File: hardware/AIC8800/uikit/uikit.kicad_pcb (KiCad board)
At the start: 2 copper layers, 50.8 x 69.2 mm, 50 parts, among them J1 Conn_01x20, J2 Conn_01x20, J3 Conn_01x10, J4 Conn_01x06, J5 USB_C_Receptacle_USB2.0, J6 Micro_SD_Card_Det, J7 PJ-393-USA, J8 Conn_01x02, SW0 SW_Push, U1 AIC1000A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

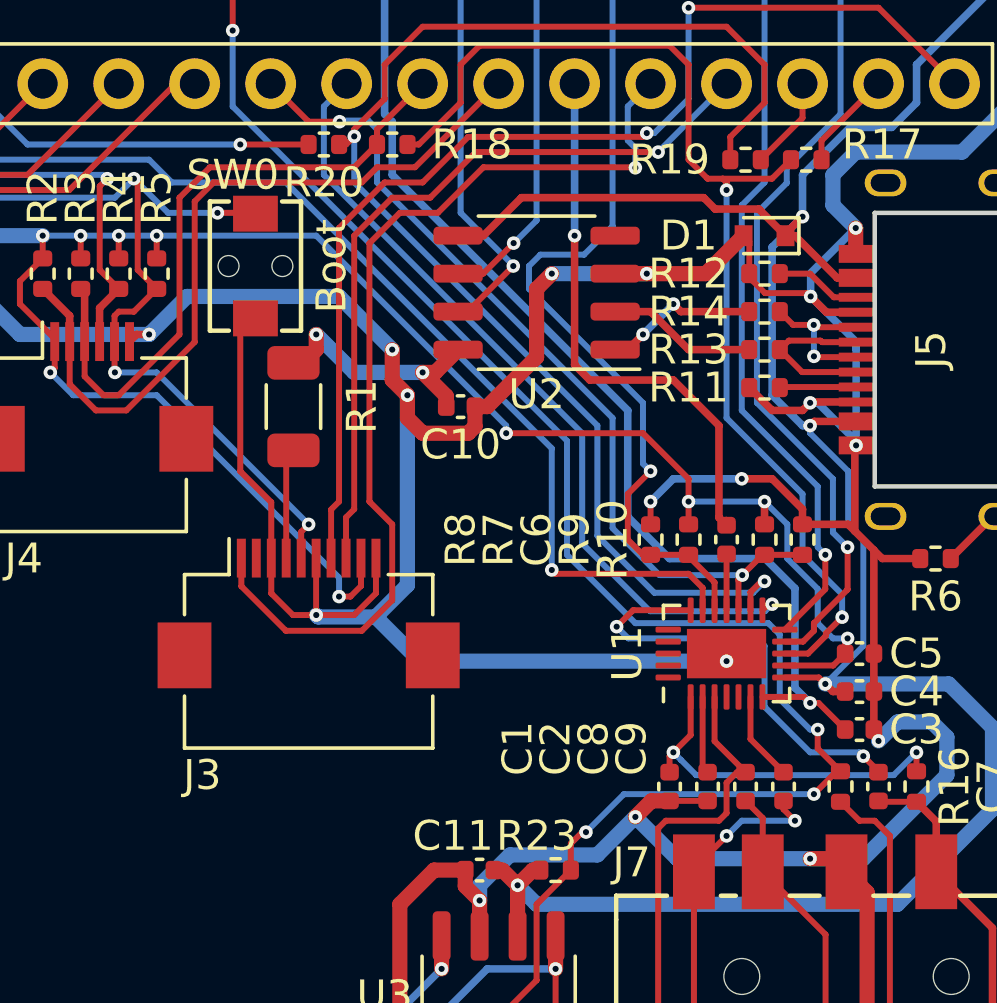
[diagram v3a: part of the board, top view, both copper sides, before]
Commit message: [hardware/aic8800m/uikit] add pin for debug uart
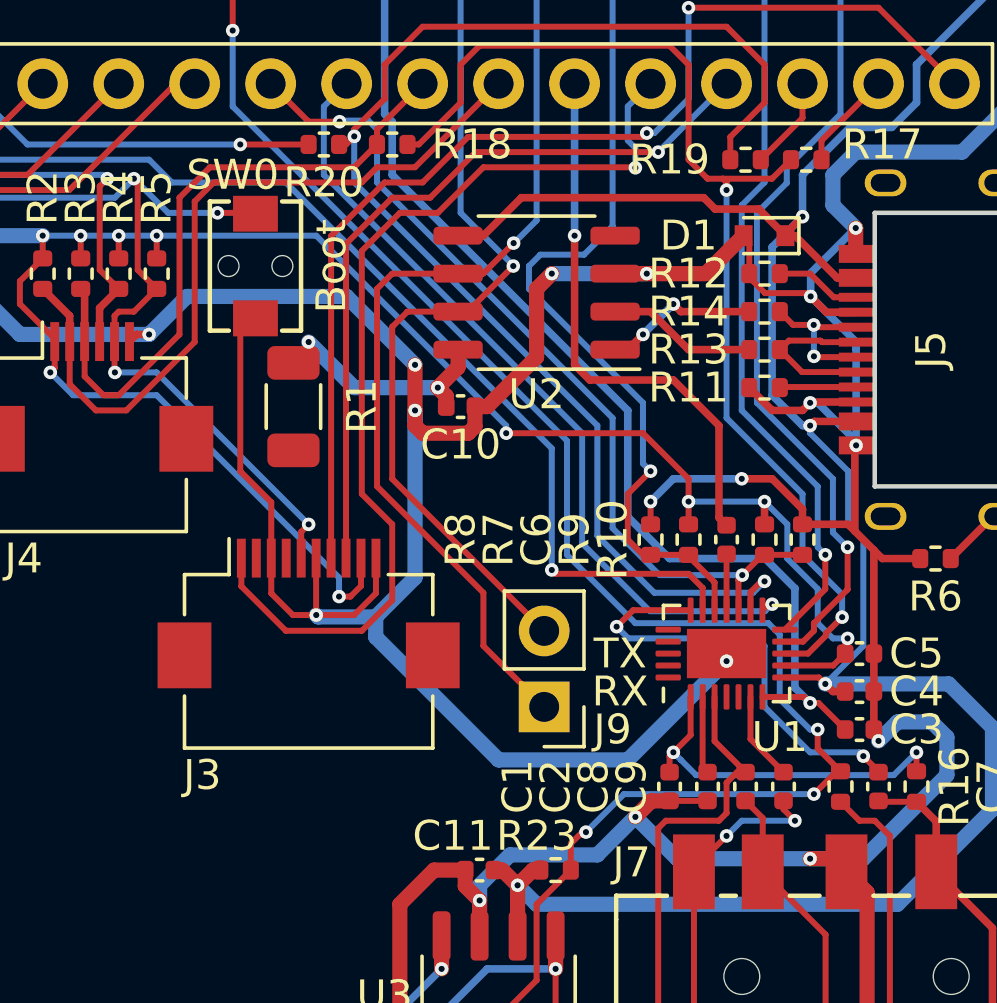
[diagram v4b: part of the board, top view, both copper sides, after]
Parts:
- added J9: Conn_01x02, Connector_PinHeader_2.54mm:PinHeader_1x02_P2.54mm_Vertical, F.Cu at (236.5, 136.4)
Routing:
- net /B2: track 33.9 -> 53.1 mm
- net /B3: track 35.3 -> 49.9 mm
- net /BL_A: track 3.70 -> 0.00 mm
- net GND: track 255.7 -> 258.6 mm
- net /USB_3V: track 8.51 -> 7.25 mm
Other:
- board text added: "RX"
- board text added: "TX"

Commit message: [hardware/aic8800m/uikit] update
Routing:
- net /BL_A: track 0.00 -> 3.70 mm
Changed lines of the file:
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@@
   (segment (start 212.09 115.57) (end 207.237 120.423) (width 0.2) (layer "F.Cu") (net 46))
   (segment (start 207.237 120.423) (end 204.354 120.423) (width 0.2) (layer "F.Cu") (net 46))
+  (segment (start 227.85 128.0695) (end 228.092 127.8275) (width 0.2) (layer "F.Cu") (net 49))
+  (segment (start 227.85 131.43) (end 227.85 128.0695) (width 0.2) (layer "F.Cu") (net 49))
   (segment (start 246.154 122.71) (end 246.9011 122.71) (width 0.2) (layer "F.Cu") (net 50))
   (segment (start 245.364 121.92) (end 246.154 122.71) (width 0.2) (layer "F.Cu") (net 50))

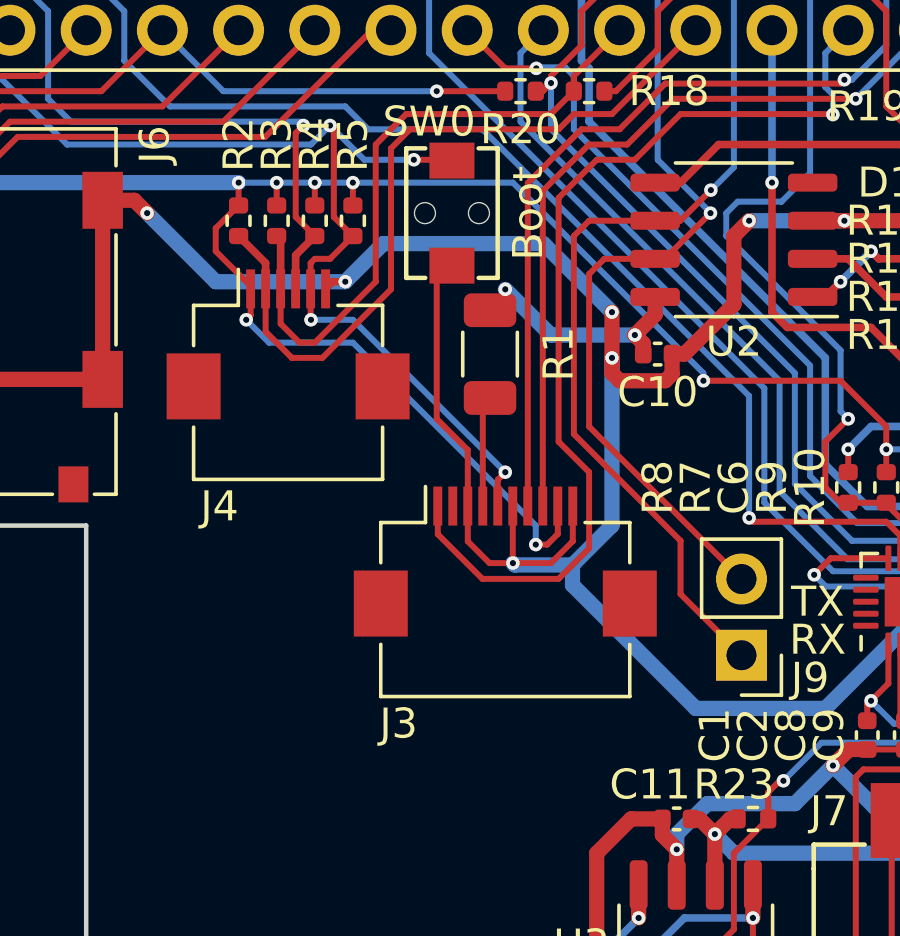
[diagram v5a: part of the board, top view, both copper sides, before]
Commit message: [hardware/aic8800m/uikit] update position of J3
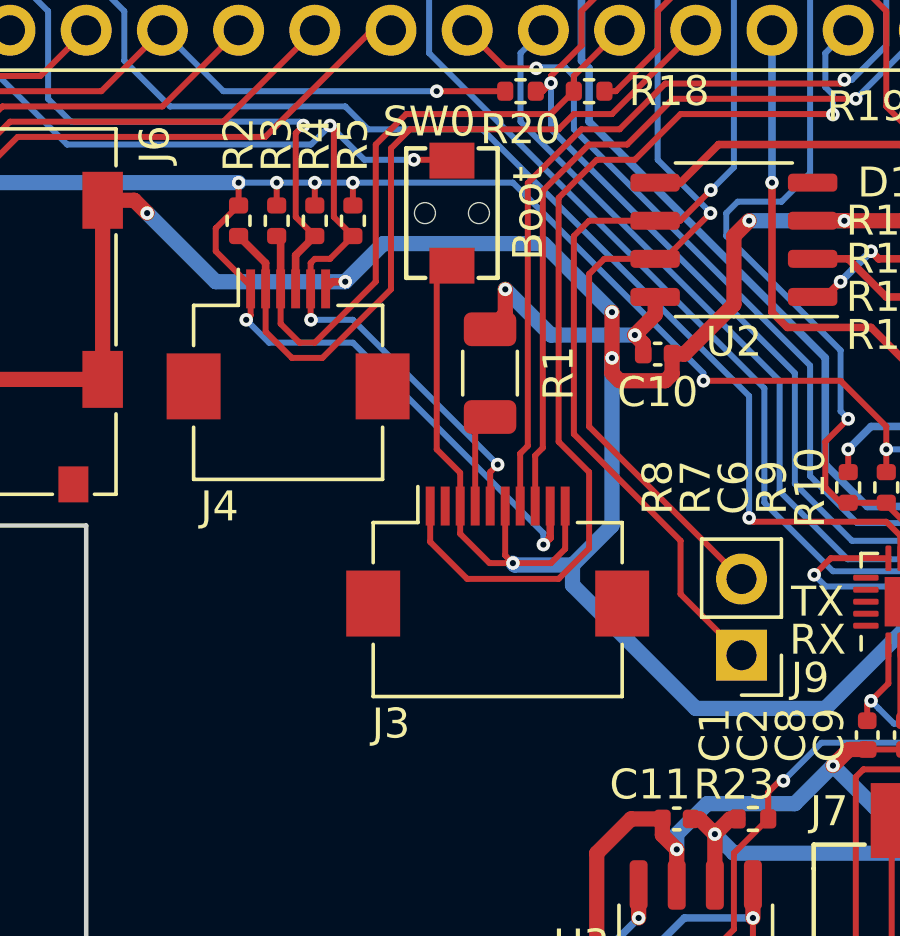
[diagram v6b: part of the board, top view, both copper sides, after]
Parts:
- moved R1 0.64 mm to (228.1, 127.0)
- moved J3 0.25 mm to (228.3, 133.3)
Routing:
- net /USB_3V: track 7.25 -> 8.79 mm
- net /BL_A: track 3.70 -> 3.17 mm

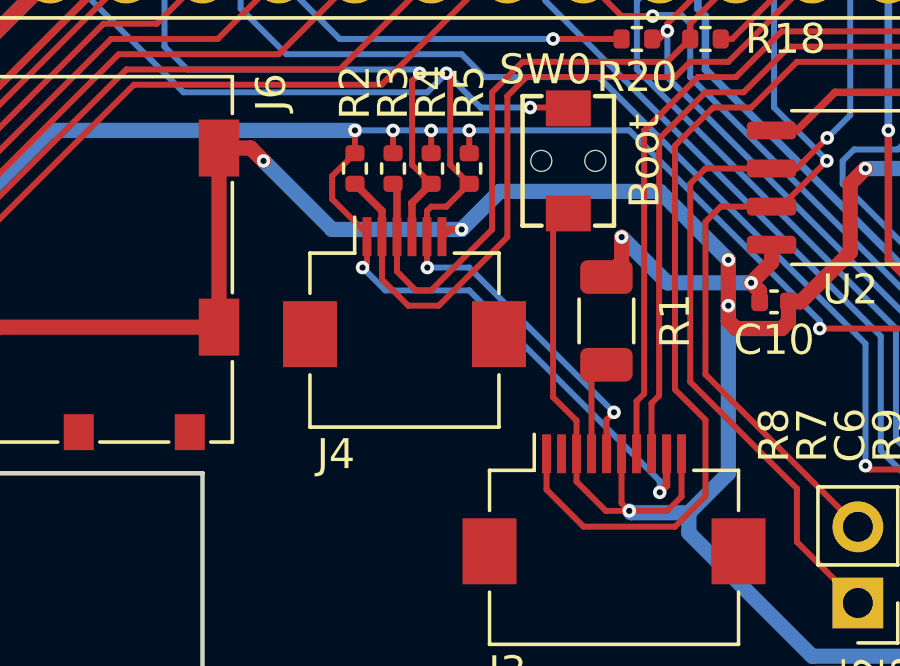
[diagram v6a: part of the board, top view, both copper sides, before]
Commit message: [hardware/aic8800m/uikit] update position of J3
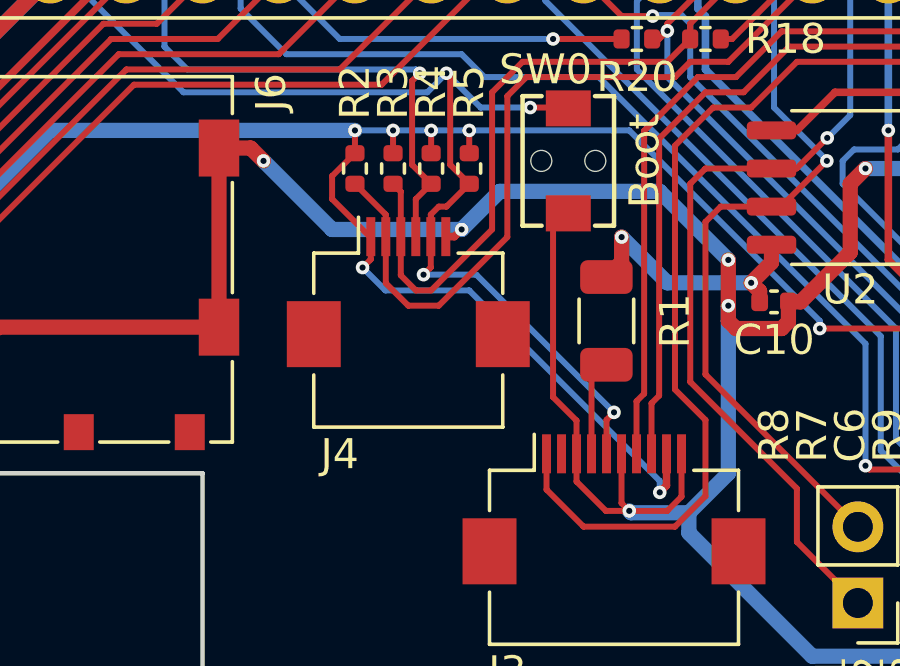
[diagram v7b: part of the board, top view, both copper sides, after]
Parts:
- moved J4 0.13 mm to (221.5, 126.1)
